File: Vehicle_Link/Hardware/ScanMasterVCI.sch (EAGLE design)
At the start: 97 parts, among them IC1 XMEGA32A4U, IC2 TL331, IC3 TL331, Q1 MMBT4403, Q10 ZXMP6A17G, Q2 MMBT3904, Q3 MMBT3904, Q4 MMBT4403, Q7 MMBT3904, Q8 MMBT4403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

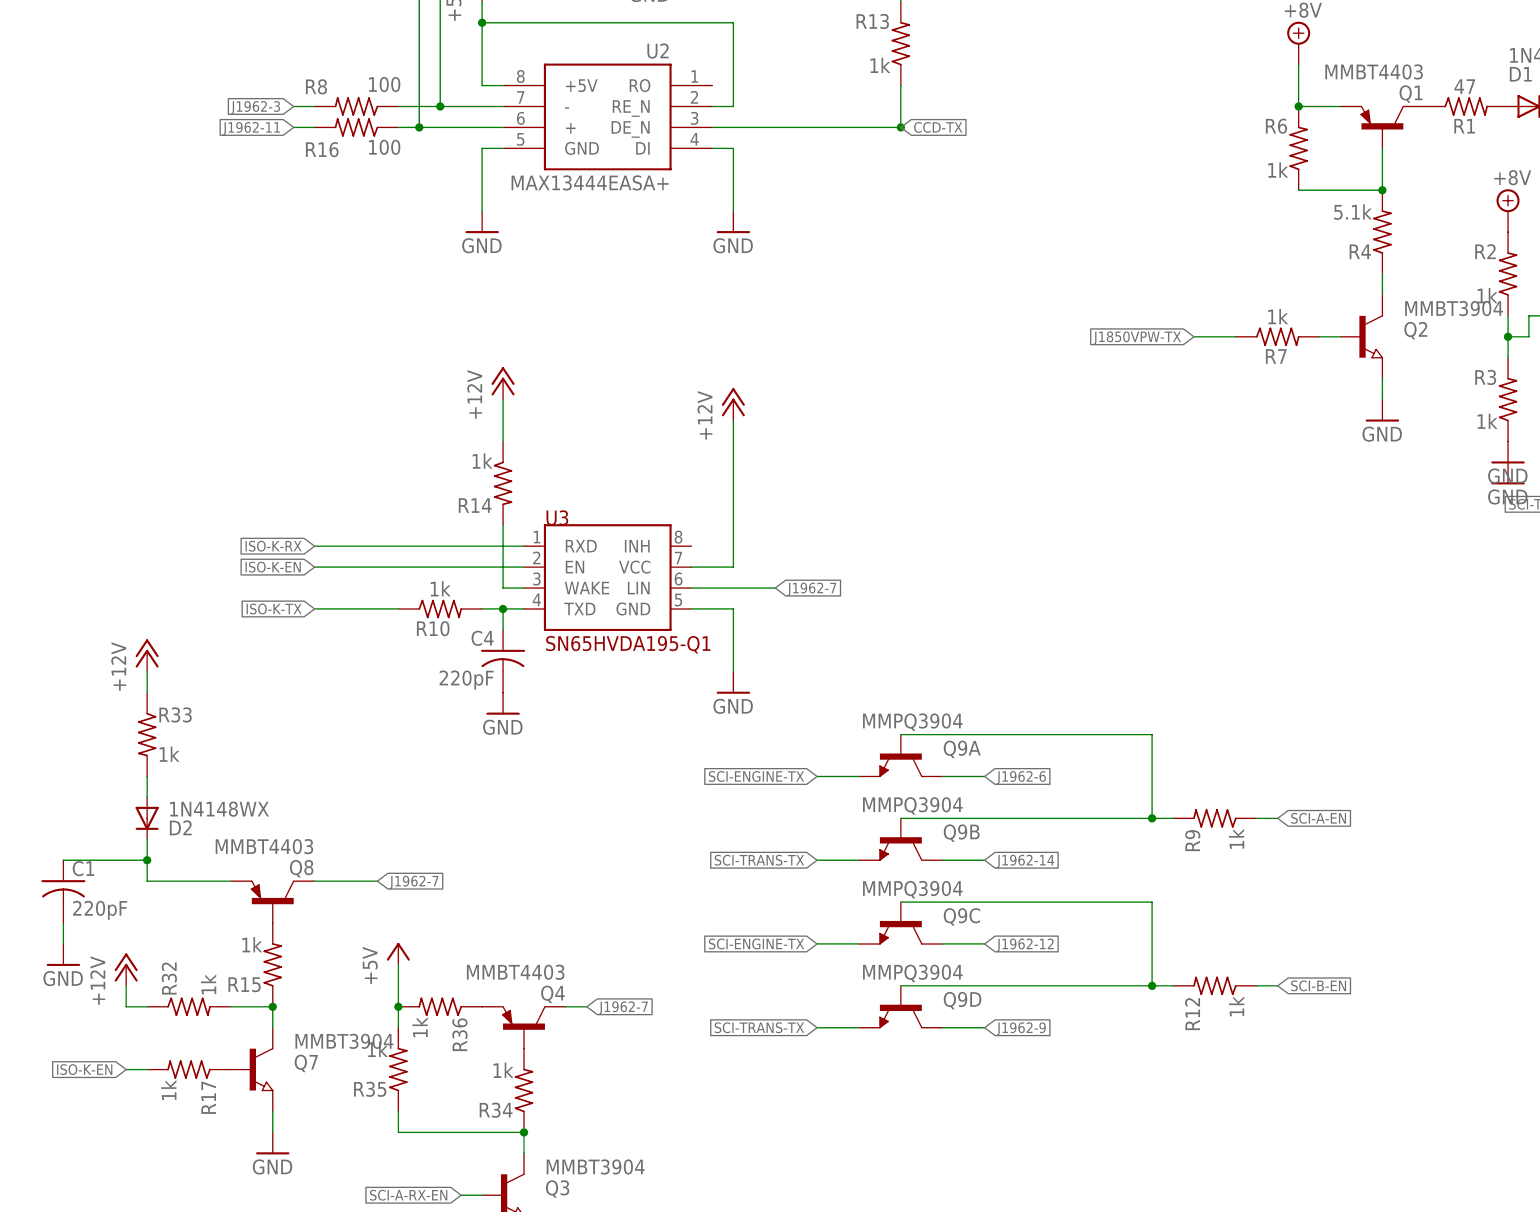
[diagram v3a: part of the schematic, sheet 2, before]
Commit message: Some more minor changes to the schematic, some pull-up resistors needed to be moved for proper transistor-enabled pull-up resistor action. Tested on circuit, working OK now.
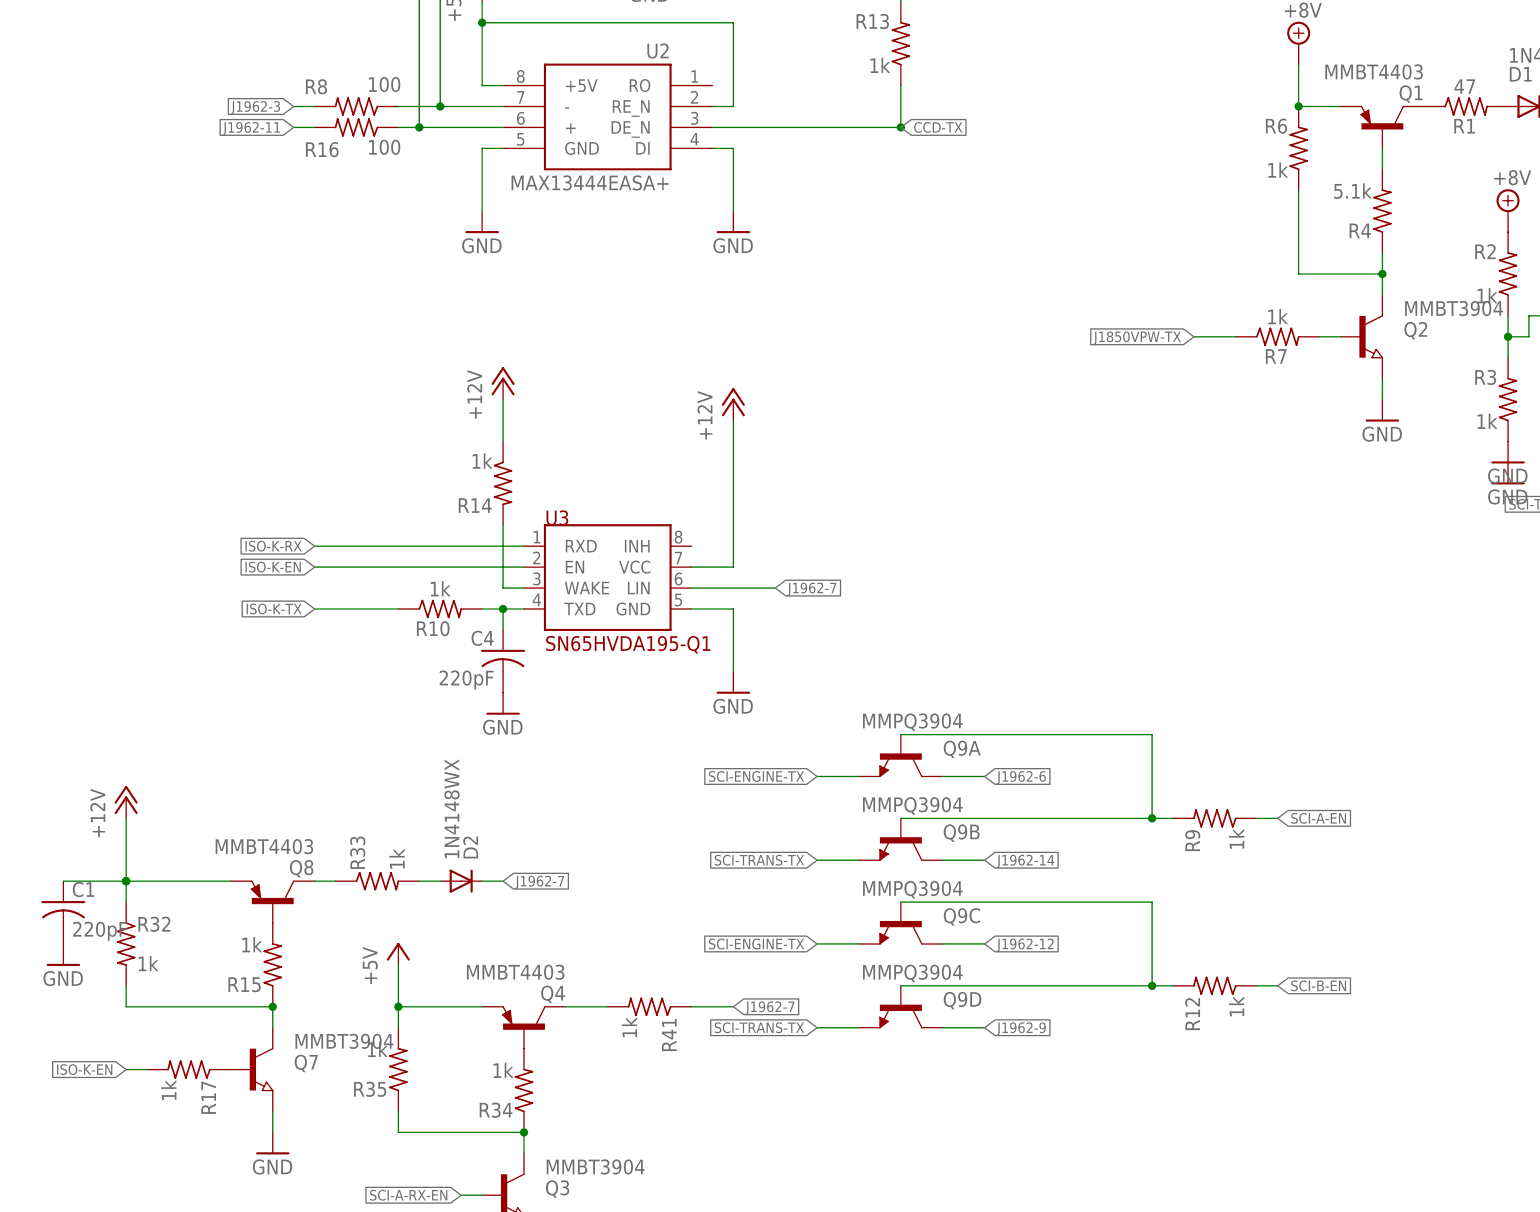
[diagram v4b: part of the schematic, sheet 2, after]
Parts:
- removed R36: 1k, adafruit:R-US_R0603
- added R41: 1k, adafruit:R-US_R0603
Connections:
- removed net N$21: C1.1, D2.C, Q8.E
- new net N$32: Q8.C, R33.1
- net +12V: now also C1.1, Q8.E; no longer R33.1
- net +5V: now also Q4.E; no longer R36.2
- net J1962-7: now also D2.C, R41.1; no longer Q4.C, Q8.C
- net N$26: now also R6.1
- net N$28: no longer R6.1
- net N$31: now also Q4.C, R41.2; no longer Q4.E, R36.1
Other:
- moved on the sheet: C1, D2, R32, R33, R4

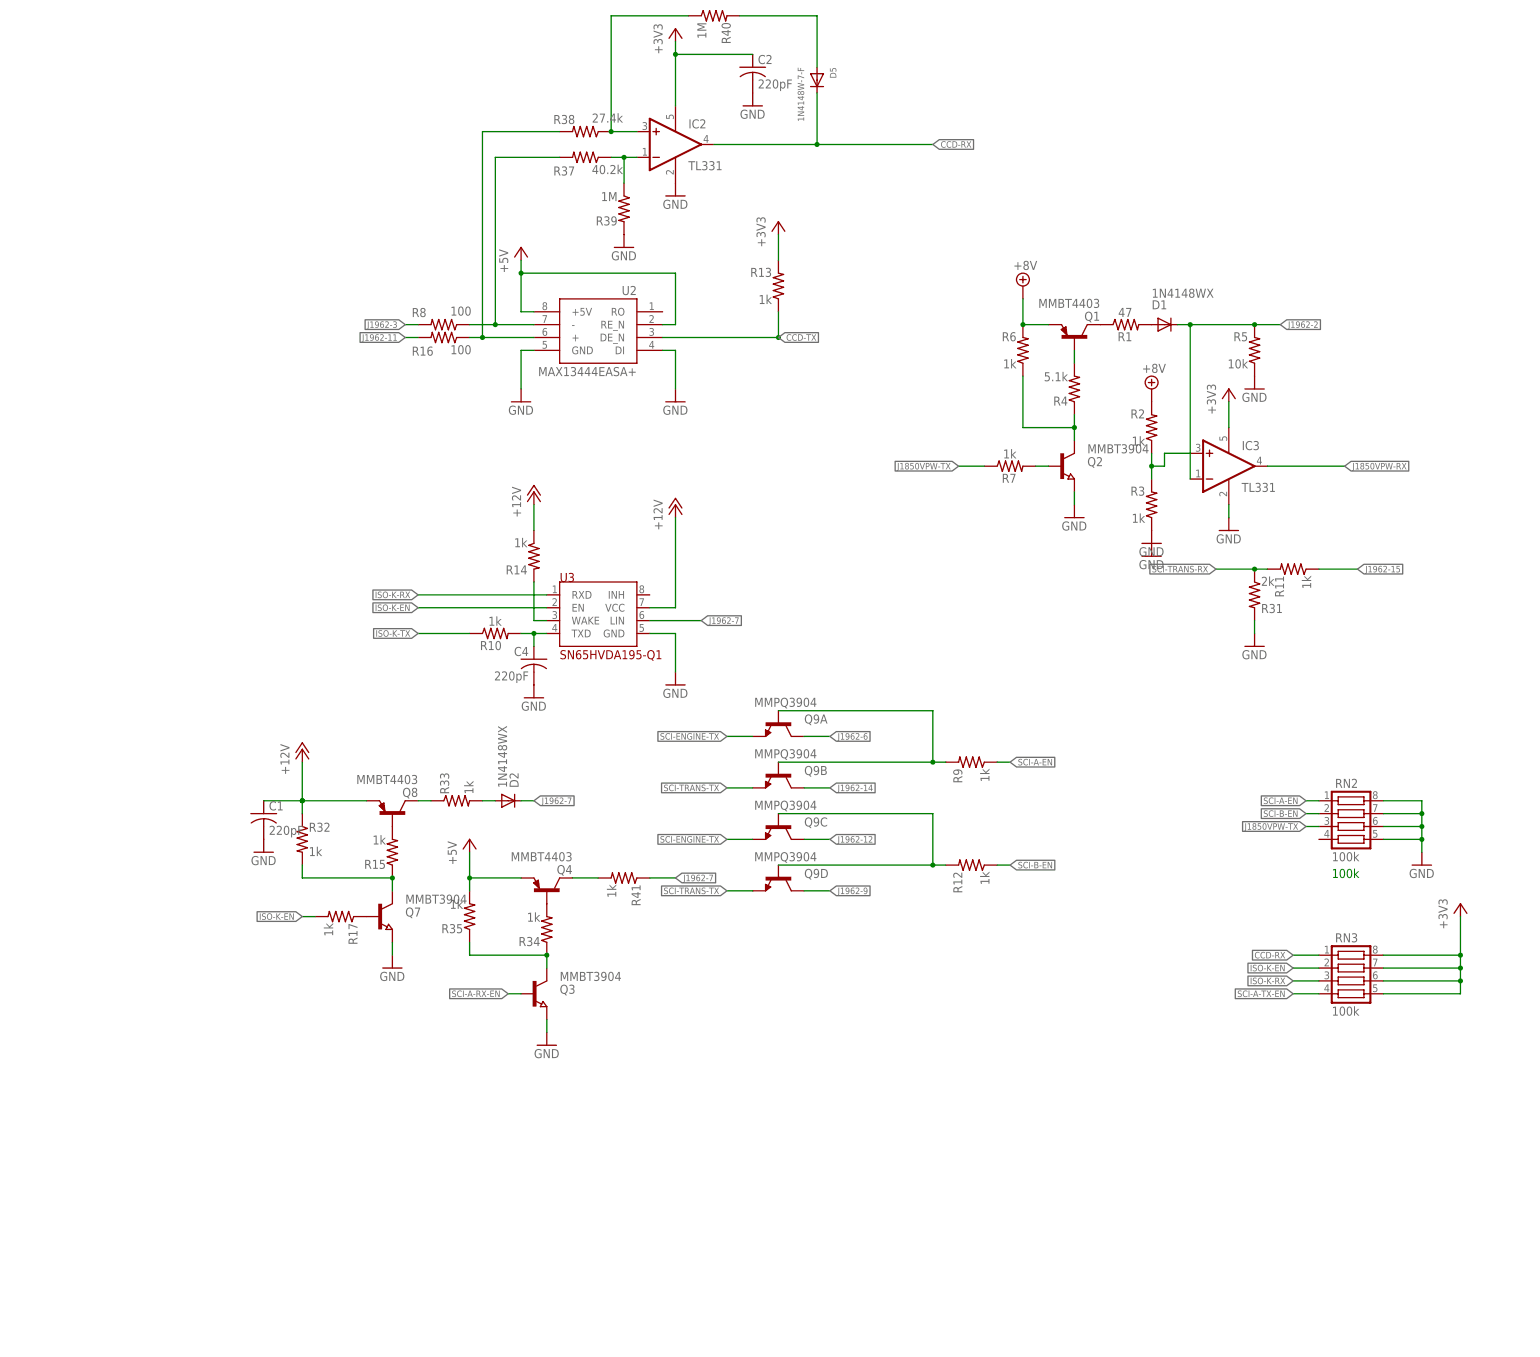
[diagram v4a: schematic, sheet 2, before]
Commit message: Started experimenting with MOSFETs, added new parts to the library for the connector I'm planning on using.
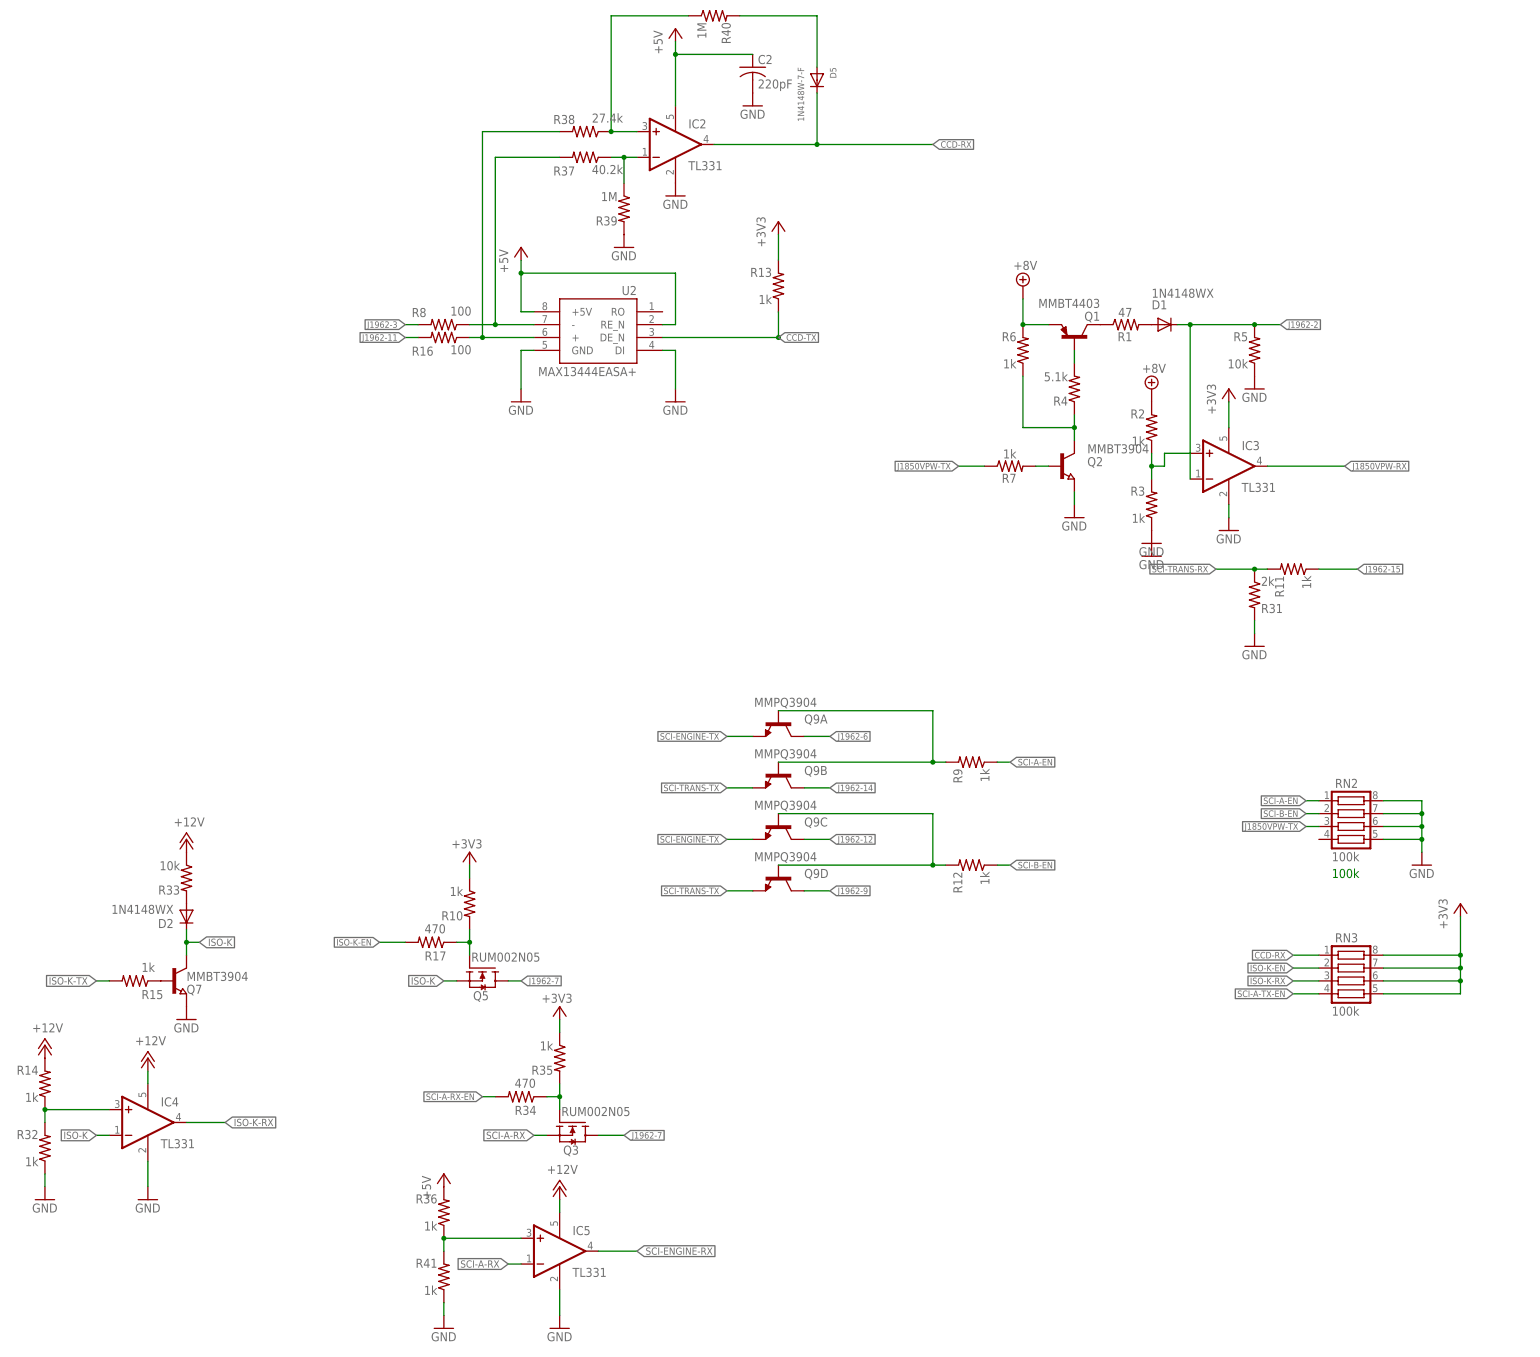
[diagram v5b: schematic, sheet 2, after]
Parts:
- removed C1, C4: 220pF, adafruit:C-USC0603
- removed Q4, Q8: MMBT4403, transistor-pnp:MMBT4403LT1SMD
- removed U3: SN65HVDA195-Q1, customics:SN65HVDA195-Q1
- added IC4, IC5: TL331, linear:TL331
- added Q5: RUM002N05, customics:RUM002N05
- added R36: 1k, adafruit:R-US_R0603
- Q3: value MMBT3904 -> RUM002N05; device semicon-smd-ipc:NPN-TRANSISTOR_SOT23 -> customics:RUM002N05
- R17, R34: value 1k -> 470
- R33: value 1k -> 10k
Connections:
- removed net N$22: Q4.B, R34.2
- removed net N$23: Q3.C, R34.1, R35.1
- removed net N$31: Q4.C, R41.2
- removed net N$32: Q8.C, R33.1
- new net ISO-K: D2.C, IC4.-IN, Q5.S, Q7.C
- new net SCI-A-RX: IC5.-IN, Q3.S
- net +12V: now also IC4.V+, IC5.V+, R14.2, R33.1; no longer C1.1, Q8.E, R14.1, R32.1, U3.VCC
- net +3V3: now also R10.1, R35.1; no longer C2.1, IC2.V+
- net +5V: now also C2.1, IC2.V+, R36.2; no longer Q4.E, R35.2
- net GND: now also IC4.GND, IC5.GND, R32.1, R41.1; no longer C1.2, C4.2, Q3.E, U3.GND
- net ISO-K-EN: no longer U3.EN
- net ISO-K-RX: now also IC4.OUT; no longer U3.RXD
- net ISO-K-TX: now also R15.2; no longer R10.1
- net J1962-7: now also Q3.D, Q5.D; no longer D2.C, R41.1, U3.LIN
- net N$10: now also Q3.G, R34.1, R35.2; no longer C4.1, R10.2, U3.TXD
- net N$13: now also R15.1; no longer R17.1
- net N$14: now also IC5.+IN, R36.1, R41.2; no longer R14.2, U3.WAKE
- net N$4: now also Q5.G, R10.2, R17.1; no longer Q7.C, R15.1, R32.2
- net N$8: now also IC4.+IN, R14.1, R32.2; no longer Q8.B, R15.2
- net SCI-A-RX-EN: now also R34.2; no longer Q3.B
- net SCI-ENGINE-RX: now also IC5.OUT
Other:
- moved on the sheet: D2, Q7, R10, R14, R15, R17, R32, R33, R34, R35, R41
